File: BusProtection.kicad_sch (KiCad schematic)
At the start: 106 parts

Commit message: Finished v03 routing
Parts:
- removed Q? (x2): MMDT2907, Package_TO_SOT_SMD:SOT-363_SC-70-6, symbol mainboard:MMDT2907
- removed Q?: MMBT2907, Package_TO_SOT_SMD:SOT-23, symbol mainboard:MMBT2907
- removed R? (x2): 0, Resistor_SMD:R_0603_1608Metric, symbol Device:R_US
- removed R? (x2): 1K, Resistor_SMD:R_0603_1608Metric, symbol Device:R_US
- removed R?: 4.7k, Resistor_SMD:R_0603_1608Metric, symbol Device:R_US
- added Q18, Q19: MMBT2907, Package_TO_SOT_SMD:SOT-23, symbol mainboard:MMBT2907
- Q10, Q11, Q14, Q15, Q2, Q3, Q6, Q7: renamed from Q?; footprint mainboard:BSS138DWQ-7 -> Package_TO_SOT_SMD:SOT-363_SC-70-6
- gave numbers to parts that had none: 74
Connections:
- net SCL is gone; now on net SCL1: R53.2, R55.2, R57.2, R59.2
- net SDA is gone; now on net SDA1: R54.2, R56.2, R58.2, R60.2
- net SD_CS is gone; now on net RF_CS: R84.2
- net SD_MISO is gone; now on net RF_MISO: R71.1, R81.2
- net SD_MOSI is gone; now on net RF_MOSI: R87.1
- net SD_SCK is gone; now on net RF_SCK: R86.1
- net FLASH_MISO: now also Q19.3 (C)
- net FLASH_MOSI: now also R89.1
- net FLASH_SCK: now also R88.2
- net F_CS: now also R85.2
- net F_MISO: now also R82.2
- net F_MOSI: now also R89.2
- net F_SCK: now also R88.1
- net MISO: now also Q18.3 (C)
- net MOSI: no longer R89.1
- net RF_CS: no longer R85.2
- net RF_MISO: no longer R82.2
- net RF_MOSI: no longer R89.2
- net RF_SCK: no longer R88.1
- net SCK: no longer R88.2
- net at R81.1: now also Q18.2 (E)
- net at R82.1: now also Q19.2 (E)
- net at R85.1: now also Q19.1 (B)
- net at R84.1: now also Q18.1 (B)
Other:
- note removed: "SPI Bus Protection - SD Card"
- moved on the sheet: R71, R88, R89

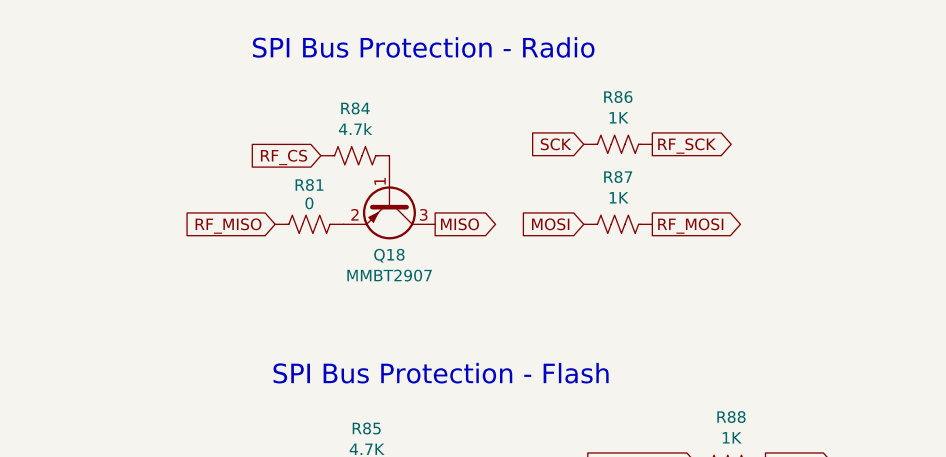
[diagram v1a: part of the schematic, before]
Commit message: Moved Batteryboard connector to avoid solder interference
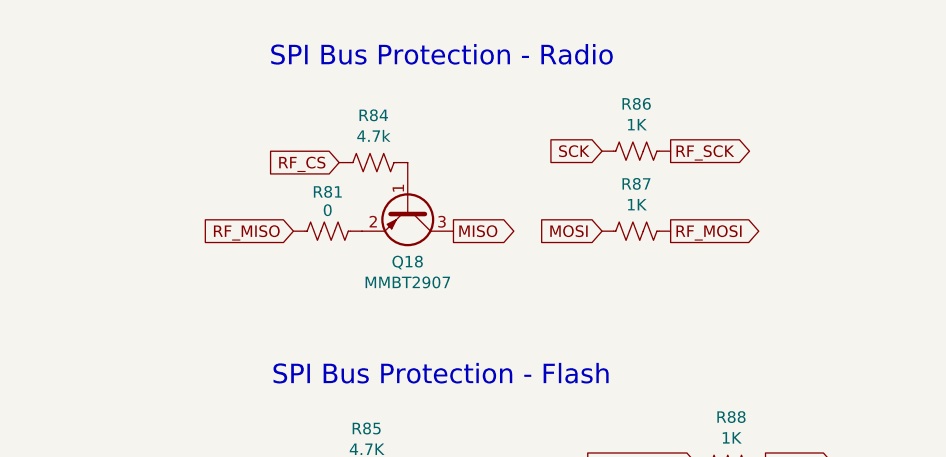
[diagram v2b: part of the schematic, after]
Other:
- moved on the sheet: Q18, R81, R84, R86, R87
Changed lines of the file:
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@@
   (title_block
     (title "PyCubed Mini")
-    (date "2022-05-09")
-    (rev "03")
+    (date "2022-06-26")
+    (rev "04.1")
     (company "RExLab Carnegie Mellon University")
     (comment 1 "Z. Manchester")
@@
     (effects (font (size 3.9878 3.9878) (thickness 0.7976) bold) (justify left bottom))
   )
-  (text "SPI Bus Protection - Radio" (at 284.226 34.29 0)
+  (text "SPI Bus Protection - Radio" (at 286.258 35.052 0)
     (effects (font (size 2.159 2.159)) (justify left bottom))
   )
@@
     )
   )
-  (global_label "SCK" (shape input) (at 321.183 43.434 180) (fields_autoplaced)
+  (global_label "SCK" (shape input) (at 323.215 44.196 180) (fields_autoplaced)
     (effects (font (size 1.27 1.27)) (justify right))
-    (property "Intersheet References" "${INTERSHEET_REFS}" (id 0) (at 87.503 12.954 0)
+    (property "Intersheet References" "${INTERSHEET_REFS}" (id 0) (at 89.535 13.716 0)
       (effects (font (size 1.27 1.27)) hide)
     )
@@
     )
   )
-  (global_label "RF_MOSI" (shape output) (at 328.803 52.324 0) (fields_autoplaced)
+  (global_label "RF_MOSI" (shape output) (at 330.835 53.086 0) (fields_autoplaced)
     (effects (font (size 1.27 1.27)) (justify left))
-    (property "Intersheet References" "${INTERSHEET_REFS}" (id 0) (at 339.0496 52.2446 0)
+    (property "Intersheet References" "${INTERSHEET_REFS}" (id 0) (at 341.0816 53.0066 0)
       (effects (font (size 1.27 1.27)) (justify left) hide)
     )
@@
     )
   )
-  (global_label "RF_SCK" (shape output) (at 328.803 43.434 0) (fields_autoplaced)
+  (global_label "RF_SCK" (shape output) (at 330.835 44.196 0) (fields_autoplaced)
     (effects (font (size 1.27 1.27)) (justify left))
-    (property "Intersheet References" "${INTERSHEET_REFS}" (id 0) (at 338.2029 43.3546 0)
+    (property "Intersheet References" "${INTERSHEET_REFS}" (id 0) (at 340.2349 44.1166 0)
       (effects (font (size 1.27 1.27)) (justify left) hide)
     )
@@
     )
   )
-  (global_label "MISO" (shape output) (at 304.673 52.324 0) (fields_autoplaced)
+  (global_label "MISO" (shape output) (at 306.705 53.086 0) (fields_autoplaced)
     (effects (font (size 1.27 1.27)) (justify left))
-    (property "Intersheet References" "${INTERSHEET_REFS}" (id 0) (at 87.503 12.954 0)
+    (property "Intersheet References" "${INTERSHEET_REFS}" (id 0) (at 89.535 13.716 0)
       (effects (font (size 1.27 1.27)) hide)
     )
@@
     )
   )
-  (global_label "RF_CS" (shape input) (at 291.973 44.704 180) (fields_autoplaced)
+  (global_label "RF_CS" (shape input) (at 294.005 45.466 180) (fields_autoplaced)
     (effects (font (size 1.27 1.27)) (justify right))
-    (property "Intersheet References" "${INTERSHEET_REFS}" (id 0) (at 283.8431 44.6246 0)
+    (property "Intersheet References" "${INTERSHEET_REFS}" (id 0) (at 285.8751 45.3866 0)
       (effects (font (size 1.27 1.27)) (justify right) hide)
     )
@@
     )
   )
-  (global_label "MOSI" (shape input) (at 321.183 52.324 180) (fields_autoplaced)
+  (global_label "MOSI" (shape input) (at 323.215 53.086 180) (fields_autoplaced)
     (effects (font (size 1.27 1.27)) (justify right))
-    (property "Intersheet References" "${INTERSHEET_REFS}" (id 0) (at 87.503 12.954 0)
+    (property "Intersheet References" "${INTERSHEET_REFS}" (id 0) (at 89.535 13.716 0)
       (effects (font (size 1.27 1.27)) hide)
     )
@@
     )
   )
-  (global_label "RF_MISO" (shape input) (at 286.893 52.324 180) (fields_autoplaced)
+  (global_label "RF_MISO" (shape input) (at 288.925 53.086 180) (fields_autoplaced)
     (effects (font (size 1.27 1.27)) (justify right))
-    (property "Intersheet References" "${INTERSHEET_REFS}" (id 0) (at 276.6464 52.2446 0)
+    (property "Intersheet References" "${INTERSHEET_REFS}" (id 0) (at 278.6784 53.0066 0)
       (effects (font (size 1.27 1.27)) (justify right) hide)
     )
@@
     (pin "2")
   )
-  (symbol (lib_id "Device:R_US") (at 324.993 52.324 270) (unit 1)
+  (symbol (lib_id "Device:R_US") (at 327.025 53.086 270) (unit 1)
     (in_bom yes) (on_board yes)
-    (property "Reference" "R87" (id 0) (at 324.993 47.117 90))
-    (property "Value" "1K" (id 1) (at 324.993 49.4284 90))
-    (property "Footprint" "Resistor_SMD:R_0603_1608Metric" (id 2) (at 324.739 53.34 90)
+    (property "Reference" "R87" (id 0) (at 327.025 47.879 90))
+    (property "Value" "1K" (id 1) (at 327.025 50.1904 90))
+    (property "Footprint" "Resistor_SMD:R_0603_1608Metric" (id 2) (at 326.771 54.102 90)
       (effects (font (size 1.27 1.27)) hide)
     )
-    (property "Datasheet" "" (id 3) (at 324.993 52.324 0)
+    (property "Datasheet" "" (id 3) (at 327.025 53.086 0)
       (effects (font (size 1.27 1.27)) hide)
     )
-    (property "Description" "1K 0603" (id 4) (at 328.7014 54.0512 0)
+    (property "Description" "1K 0603" (id 4) (at 330.7334 54.8132 0)
       (effects (font (size 1.27 1.27)) hide)
     )
@@
     (pin "2")
   )
-  (symbol (lib_id "Device:R_US") (at 290.703 52.324 270) (unit 1)
+  (symbol (lib_id "Device:R_US") (at 292.735 53.086 270) (unit 1)
     (in_bom yes) (on_board yes)
-    (property "Reference" "R81" (id 0) (at 290.703 48.006 90))
-    (property "Value" "0" (id 1) (at 290.703 50.038 90))
-    (property "Footprint" "Resistor_SMD:R_0603_1608Metric" (id 2) (at 290.449 53.34 90)
+    (property "Reference" "R81" (id 0) (at 292.735 48.768 90))
+    (property "Value" "0" (id 1) (at 292.735 50.8 90))
+    (property "Footprint" "Resistor_SMD:R_0603_1608Metric" (id 2) (at 292.481 54.102 90)
       (effects (font (size 1.27 1.27)) hide)
     )
-    (property "Datasheet" "" (id 3) (at 290.703 52.324 0)
+    (property "Datasheet" "" (id 3) (at 292.735 53.086 0)
       (effects (font (size 1.27 1.27)) hide)
     )
-    (property "Description" "0 0603" (id 4) (at 293.243 47.117 0)
+    (property "Description" "0 0603" (id 4) (at 295.275 47.879 0)
       (effects (font (size 1.27 1.27)) hide)
     )
@@
     (pin "2")
   )
-  (symbol (lib_id "mainboard:MMBT2907") (at 299.593 49.784 270) (unit 1)
+  (symbol (lib_id "mainboard:MMBT2907") (at 301.625 50.546 270) (unit 1)
     (in_bom yes) (on_board yes)
-    (property "Reference" "Q18" (id 0) (at 299.593 55.753 90))
-    (property "Value" "MMBT2907" (id 1) (at 299.593 58.0644 90))
-    (property "Footprint" "Package_TO_SOT_SMD:SOT-23" (id 2) (at 297.688 54.864 0)
+    (property "Reference" "Q18" (id 0) (at 301.625 56.515 90))
+    (property "Value" "MMBT2907" (id 1) (at 301.625 58.8264 90))
+    (property "Footprint" "Package_TO_SOT_SMD:SOT-23" (id 2) (at 299.72 55.626 0)
       (effects (font (size 1.27 1.27) italic) (justify left) hide)
     )
-    (property "Datasheet" "https://www.diodes.com/assets/Datasheets/ds30040.pdf" (id 3) (at 299.593 49.784 0)
+    (property "Datasheet" "https://www.diodes.com/assets/Datasheets/ds30040.pdf" (id 3) (at 301.625 50.546 0)
       (effects (font (size 1.27 1.27)) (justify left) hide)
     )
-    (property "Description" "Single PNP BJT" (id 4) (at 299.593 49.784 0)
+    (property "Description" "Single PNP BJT" (id 4) (at 301.625 50.546 0)
       (effects (font (size 1.27 1.27)) hide)
     )
-    (property "Flight" "MMBT2907ALT1G" (id 5) (at 299.593 49.784 0)
+    (property "Flight" "MMBT2907ALT1G" (id 5) (at 301.625 50.546 0)
       (effects (font (size 1.27 1.27)) hide)
     )
-    (property "Manufacturer_Name" "ON Semiconductor" (id 6) (at 299.593 49.784 0)
+    (property "Manufacturer_Name" "ON Semiconductor" (id 6) (at 301.625 50.546 0)
       (effects (font (size 1.27 1.27)) hide)
     )
-    (property "Manufacturer_Part_Number" "MMBT2907ALT1G" (id 7) (at 302.133 55.753 0)
+    (property "Manufacturer_Part_Number" "MMBT2907ALT1G" (id 7) (at 304.165 56.515 0)
       (effects (font (size 1.27 1.27)) hide)
     )
-    (property "Proto" "MMBT2907A" (id 8) (at 299.593 49.784 0)
+    (property "Proto" "MMBT2907A" (id 8) (at 301.625 50.546 0)
       (effects (font (size 1.27 1.27)) hide)
     )
@@
     (pin "1")
   )
-  (symbol (lib_id "Device:R_US") (at 295.783 44.704 270) (unit 1)
+  (symbol (lib_id "Device:R_US") (at 297.815 45.466 270) (unit 1)
     (in_bom yes) (on_board yes)
-    (property "Reference" "R84" (id 0) (at 295.783 39.497 90))
-    (property "Value" "4.7k" (id 1) (at 295.783 41.8084 90))
-    (property "Footprint" "Resistor_SMD:R_0603_1608Metric" (id 2) (at 295.529 45.72 90)
+    (property "Reference" "R84" (id 0) (at 297.815 40.259 90))
+    (property "Value" "4.7k" (id 1) (at 297.815 42.5704 90))
+    (property "Footprint" "Resistor_SMD:R_0603_1608Metric" (id 2) (at 297.561 46.482 90)
       (effects (font (size 1.27 1.27)) hide)
     )
-    (property "Datasheet" "" (id 3) (at 295.783 44.704 0)
+    (property "Datasheet" "" (id 3) (at 297.815 45.466 0)
       (effects (font (size 1.27 1.27)) hide)
     )
-    (property "Description" "4.7k 0603" (id 4) (at 298.323 39.497 0)
+    (property "Description" "4.7k 0603" (id 4) (at 300.355 40.259 0)
       (effects (font (size 1.27 1.27)) hide)
     )
@@
     (pin "2")
   )
-  (symbol (lib_id "Device:R_US") (at 324.993 43.434 270) (unit 1)
+  (symbol (lib_id "Device:R_US") (at 327.025 44.196 270) (unit 1)
     (in_bom yes) (on_board yes)
-    (property "Reference" "R86" (id 0) (at 324.993 38.227 90))
-    (property "Value" "1K" (id 1) (at 324.993 40.5384 90))
-    (property "Footprint" "Resistor_SMD:R_0603_1608Metric" (id 2) (at 324.739 44.45 90)
+    (property "Reference" "R86" (id 0) (at 327.025 38.989 90))
+    (property "Value" "1K" (id 1) (at 327.025 41.3004 90))
+    (property "Footprint" "Resistor_SMD:R_0603_1608Metric" (id 2) (at 326.771 45.212 90)
       (effects (font (size 1.27 1.27)) hide)
     )
-    (property "Datasheet" "" (id 3) (at 324.993 43.434 0)
+    (property "Datasheet" "" (id 3) (at 327.025 44.196 0)
       (effects (font (size 1.27 1.27)) hide)
     )
-    (property "Description" "1K 0603" (id 4) (at 328.7014 45.1612 0)
+    (property "Description" "1K 0603" (id 4) (at 330.7334 45.9232 0)
       (effects (font (size 1.27 1.27)) hide)
     )

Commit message: v05 Updates
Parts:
- added C34, C35: 10nF, Capacitor_SMD:C_0603_1608Metric, symbol Device:C
- added Q1, Q21: BSS138DWQ-7, Package_TO_SOT_SMD:SOT-363_SC-70-6, symbol mainboard:BSS138DWQ-7
- added Q20, Q22: MBT2222ADW1T1, Package_TO_SOT_SMD:SOT-363_SC-70-6, symbol Transistor_BJT:MBT2222ADW1T1
- added R100, R99: 0, Resistor_SMD:R_0603_1608Metric, symbol Device:R_US
- added R16, R94: 680, Resistor_SMD:R_0603_1608Metric, symbol Device:R_US
- added R90, R95: 100K, Resistor_SMD:R_0603_1608Metric, symbol Device:R_US
- added R91, R92, R96, R97: 10K, Resistor_SMD:R_0603_1608Metric, symbol Device:R_US
- added R93, R98: 200K, Resistor_SMD:R_0603_1608Metric, symbol Device:R_US
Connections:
- net +3V3: now also R90.1, R91.1, R92.1, R95.1, R96.1, R97.1
- net GND: now also C34.2, C35.2, Q1.1 (S2), Q1.4 (S1), Q21.1 (S2), Q21.4 (S1)
- net SCL1: now also Q20.1 (E1), Q20.3 (C2), R99.2; no longer Q4.1 (E1), Q4.3 (C2), R53.2
- net SDA1: now also Q22.1 (E1), Q22.3 (C2), R100.2; no longer Q8.1 (E1), Q8.3 (C2), R54.2
- new net: Q21.2 (G2), Q21.3 (D2), R95.2
- new net: Q22.2 (B1), R94.1
- new net: Q21.6 (D1), Q22.5 (B2), R94.2, R96.2
- new net: C35.1, Q21.5 (G1), R98.2
- new net: Q20.2 (B1), R16.1
- new net: C34.1, Q1.5 (G1), R93.2
- new net: Q1.6 (D1), Q20.5 (B2), R16.2, R91.2
- new net: Q1.2 (G2), Q1.3 (D2), R90.2
- new net SCL2: Q4.1 (E1), Q4.3 (C2), R53.2
- new net SCL_MAG: Q20.4 (E2), Q20.6 (C1), R92.2, R93.1, R99.1
- new net SDA2: Q8.1 (E1), Q8.3 (C2), R54.2
- new net SDA_MAG: Q22.4 (E2), Q22.6 (C1), R100.1, R97.2, R98.1
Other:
- note added: "I2C Bus Protection - Magnetometer"
- moved on the sheet: C24, C25, C26, C27, C28, C29, C30, C31, Q10A, Q10B, Q11A, Q11B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
